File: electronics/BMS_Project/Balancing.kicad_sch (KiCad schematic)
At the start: 20 parts, among them Q1 IRLB8721PBF, Q2 IRLB8721PBF, Q3 IRLB8721PBF, Q4 IRLB8721PBF, U3 LTV-817, U4 LTV-817, U5 LTV-817, U6 LTV-817

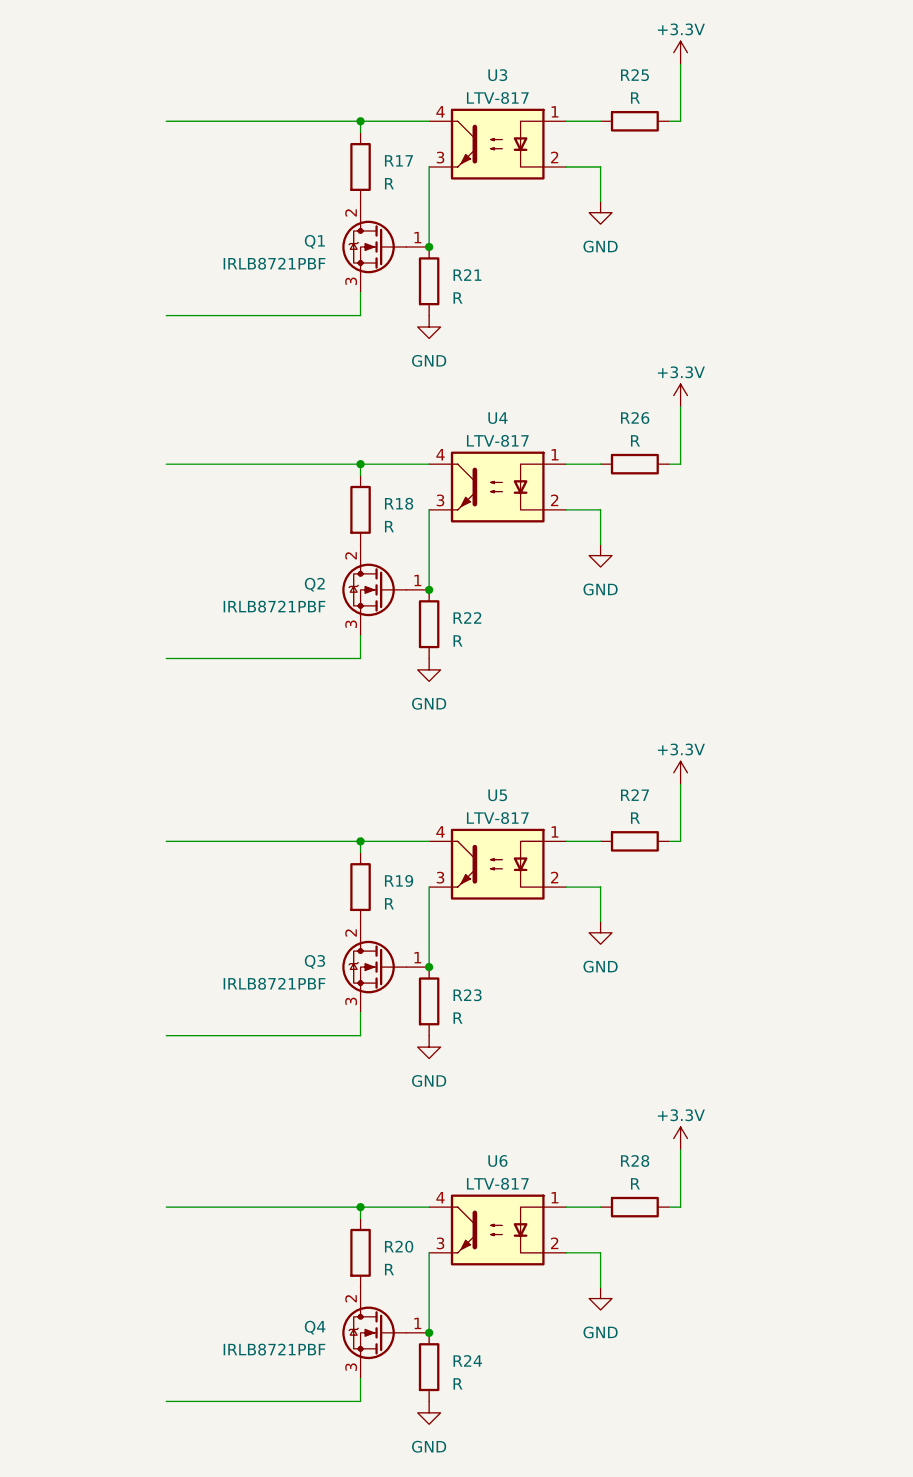
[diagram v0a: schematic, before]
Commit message: Started working on schematic segmentation and added first labels
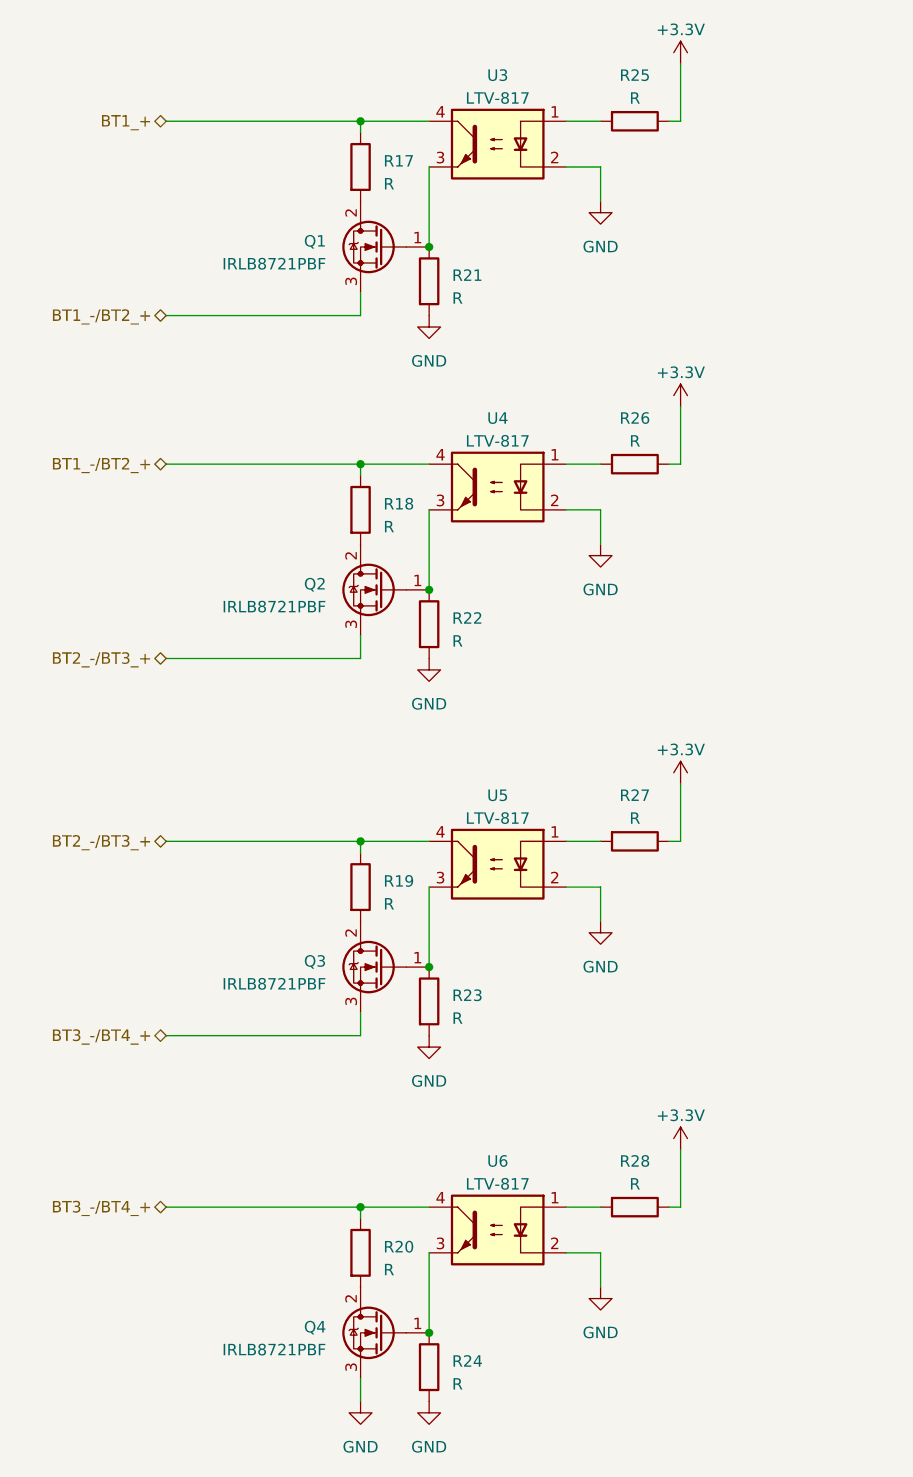
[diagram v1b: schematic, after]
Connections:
- net GND: now also Q4.3 (S)
- net BT3_-/BT4_+: now reaches R20.1, U6.4
- net BT3_-/BT4_+: now also Q3.3 (S)
- net BT2_-/BT3_+: now reaches Q2.3 (S)
- net BT2_-/BT3_+: now also R19.1, U5.4
- net BT1_-/BT2_+: now reaches R18.1, U4.4
- net BT1_-/BT2_+: now also Q1.3 (S)
- net BT1_+: now reaches R17.1, U3.4
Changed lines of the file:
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@@
-    (stroke (width 0) (type default))
-  )
-  (wire (pts (xy 114.3 173.99) (xy 92.71 173.99))
     (stroke (width 0) (type default))
   )
@@
   (wire (pts (xy 137.16 157.48) (xy 140.97 157.48))
     (stroke (width 0) (type default))
+  )
+  (hierarchical_label "BT1_-{slash}BT2_+" (shape bidirectional) (at 92.71 53.34 180) (fields_autoplaced)
+    (effects (font (size 1.27 1.27)) (justify right))
+  )
+  (hierarchical_label "BT2_-{slash}BT3_+" (shape bidirectional) (at 92.71 91.44 180) (fields_autoplaced)
+    (effects (font (size 1.27 1.27)) (justify right))
+  )
+  (hierarchical_label "BT1_+" (shape bidirectional) (at 92.71 31.75 180) (fields_autoplaced)
+    (effects (font (size 1.27 1.27)) (justify right))
+  )
+  (hierarchical_label "BT1_-{slash}BT2_+" (shape bidirectional) (at 92.71 69.85 180) (fields_autoplaced)
+    (effects (font (size 1.27 1.27)) (justify right))
+  )
+  (hierarchical_label "BT3_-{slash}BT4_+" (shape bidirectional) (at 92.71 152.4 180) (fields_autoplaced)
+    (effects (font (size 1.27 1.27)) (justify right))
+  )
+  (hierarchical_label "BT3_-{slash}BT4_+" (shape bidirectional) (at 92.71 133.35 180) (fields_autoplaced)
+    (effects (font (size 1.27 1.27)) (justify right))
+  )
+  (hierarchical_label "BT2_-{slash}BT3_+" (shape bidirectional) (at 92.71 111.76 180) (fields_autoplaced)
+    (effects (font (size 1.27 1.27)) (justify right))
   )
   (symbol (lib_id "Device:R") (at 121.92 49.53 0) (unit 1)
@@
         )
       )
+    )
+  )
+  (symbol (lib_id "power:GND") (at 114.3 173.99 0) (unit 1)
+    (in_bom yes) (on_board yes) (dnp no) (fields_autoplaced)
+    (property "Reference" "#PWR013" (at 114.3 180.34 0)
+      (effects (font (size 1.27 1.27)) hide)
+    )
+    (property "Value" "GND" (at 114.3 179.07 0)
+      (effects (font (size 1.27 1.27)))
+    )
+    (property "Footprint" "" (at 114.3 173.99 0)
+      (effects (font (size 1.27 1.27)) hide)
+    )
+    (property "Datasheet" "" (at 114.3 173.99 0)
+      (effects (font (size 1.27 1.27)) hide)
+    )
+    (pin "1")
+    (instances
+      (project "BMS_Project"
+        (path "/524e7f14-feb0-4ca2-9425-a347c869bfa6/d8f12774-e346-4091-abf5-b4c43e81469c"
+          (reference "#PWR013") (unit 1)
+        )
+        (path "/524e7f14-feb0-4ca2-9425-a347c869bfa6/d60b6f2f-e13e-4849-9977-88b541f58c2b"
+          (reference "#PWR025") (unit 1)
+        )
+      )
+      (project "Test_Projekt"
+        (path "/d5b120ca-a0f0-4b3f-8fab-ca010d94ac2e"
+          (reference "#PWR03") (unit 1)
+        )
+      )

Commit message: added values to the parts
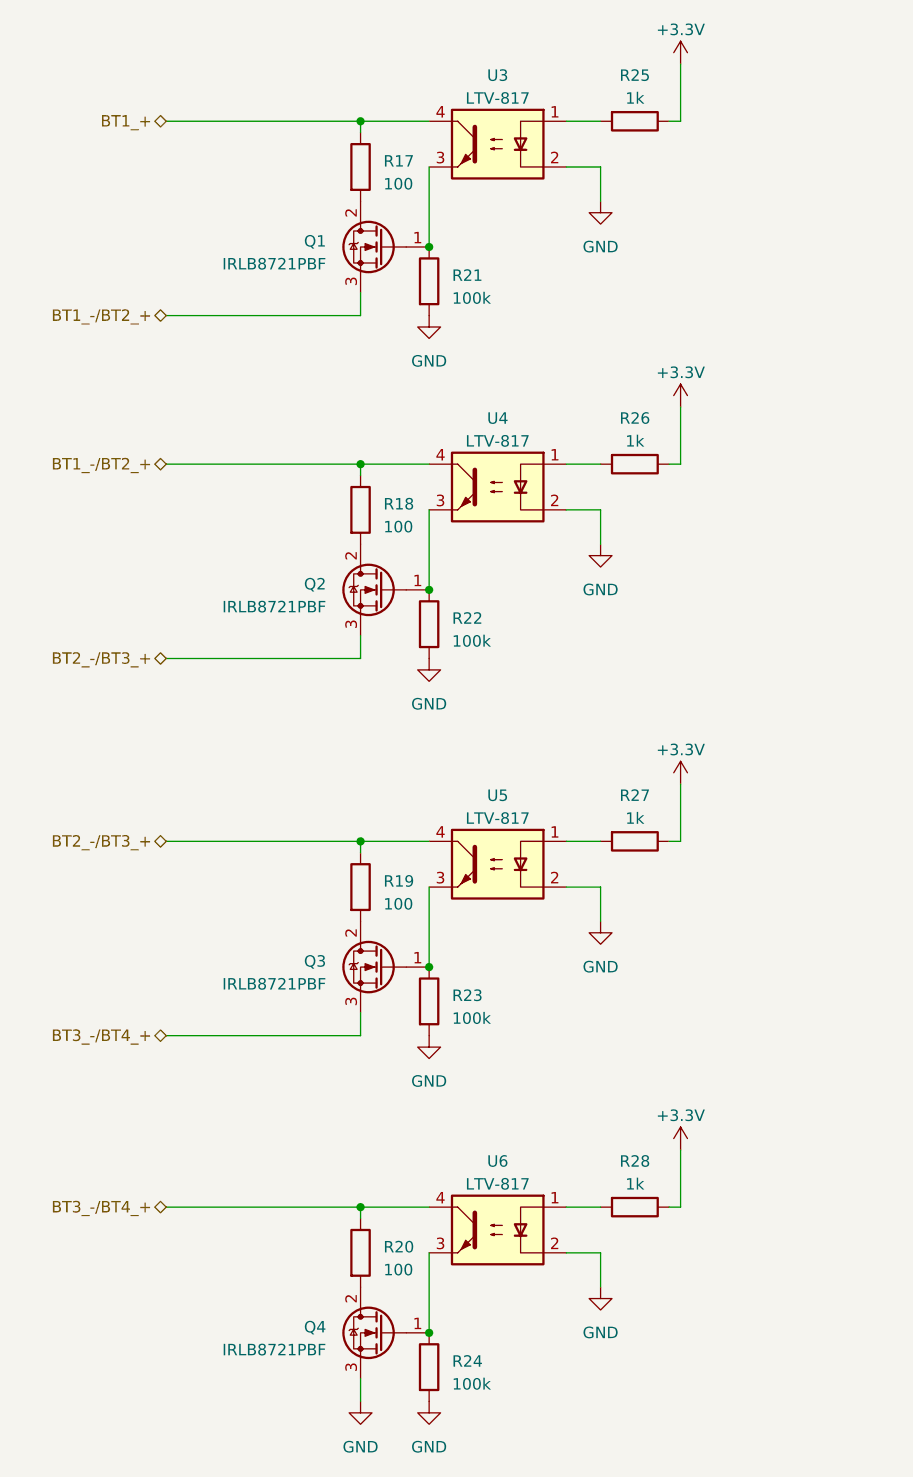
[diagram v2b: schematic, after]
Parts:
- R17, R18, R19, R20: value R -> 100
- R21, R22, R23, R24: value R -> 100k
- R25, R26, R27, R28: value R -> 1k
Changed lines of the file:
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@@
       (effects (font (size 1.27 1.27)) (justify left))
     )
-    (property "Value" "R" (at 124.46 51.435 0)
+    (property "Value" "100k" (at 124.46 51.435 0)
       (effects (font (size 1.27 1.27)) (justify left))
     )
@@
       (effects (font (size 1.27 1.27)) (justify left))
     )
-    (property "Value" "R" (at 116.84 159.385 0)
+    (property "Value" "100" (at 116.84 159.385 0)
       (effects (font (size 1.27 1.27)) (justify left))
     )
@@
       (effects (font (size 1.27 1.27)))
     )
-    (property "Value" "R" (at 144.78 29.21 90)
+    (property "Value" "1k" (at 144.78 29.21 90)
       (effects (font (size 1.27 1.27)))
     )
@@
       (effects (font (size 1.27 1.27)))
     )
-    (property "Value" "R" (at 144.78 149.86 90)
+    (property "Value" "1k" (at 144.78 149.86 90)
       (effects (font (size 1.27 1.27)))
     )
@@
       (effects (font (size 1.27 1.27)))
     )
-    (property "Value" "R" (at 144.78 67.31 90)
+    (property "Value" "1k" (at 144.78 67.31 90)
       (effects (font (size 1.27 1.27)))
     )
@@
       (effects (font (size 1.27 1.27)) (justify left))
     )
-    (property "Value" "R" (at 116.84 76.835 0)
+    (property "Value" "100" (at 116.84 76.835 0)
       (effects (font (size 1.27 1.27)) (justify left))
     )
@@
       (effects (font (size 1.27 1.27)) (justify left))
     )
-    (property "Value" "R" (at 124.46 89.535 0)
+    (property "Value" "100k" (at 124.46 89.535 0)
       (effects (font (size 1.27 1.27)) (justify left))
     )
@@
       (effects (font (size 1.27 1.27)))
     )
-    (property "Value" "R" (at 144.78 109.22 90)
+    (property "Value" "1k" (at 144.78 109.22 90)
       (effects (font (size 1.27 1.27)))
     )
@@
       (effects (font (size 1.27 1.27)) (justify left))
     )
-    (property "Value" "R" (at 116.84 118.745 0)
+    (property "Value" "100" (at 116.84 118.745 0)
       (effects (font (size 1.27 1.27)) (justify left))
     )
@@
       (effects (font (size 1.27 1.27)) (justify left))
     )
-    (property "Value" "R" (at 116.84 38.735 0)
+    (property "Value" "100" (at 116.84 38.735 0)
       (effects (font (size 1.27 1.27)) (justify left))
     )
@@
       (effects (font (size 1.27 1.27)) (justify left))
     )
-    (property "Value" "R" (at 124.46 131.445 0)
+    (property "Value" "100k" (at 124.46 131.445 0)
       (effects (font (size 1.27 1.27)) (justify left))
     )
@@
       (effects (font (size 1.27 1.27)) (justify left))
     )
-    (property "Value" "R" (at 124.46 172.085 0)
-      (effects (font (size 1.27 1.27)) (justify left))
-    )
+    (property "Value" "100k" (at 124.46 172.085 0)
+      (effects (font (size 1.27 1.27)) (justify left))
+    )
